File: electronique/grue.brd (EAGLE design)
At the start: 160 x 100 mm, 23 parts, among them IC3 REG1117, Q1 BSS138, Q2 BSS138

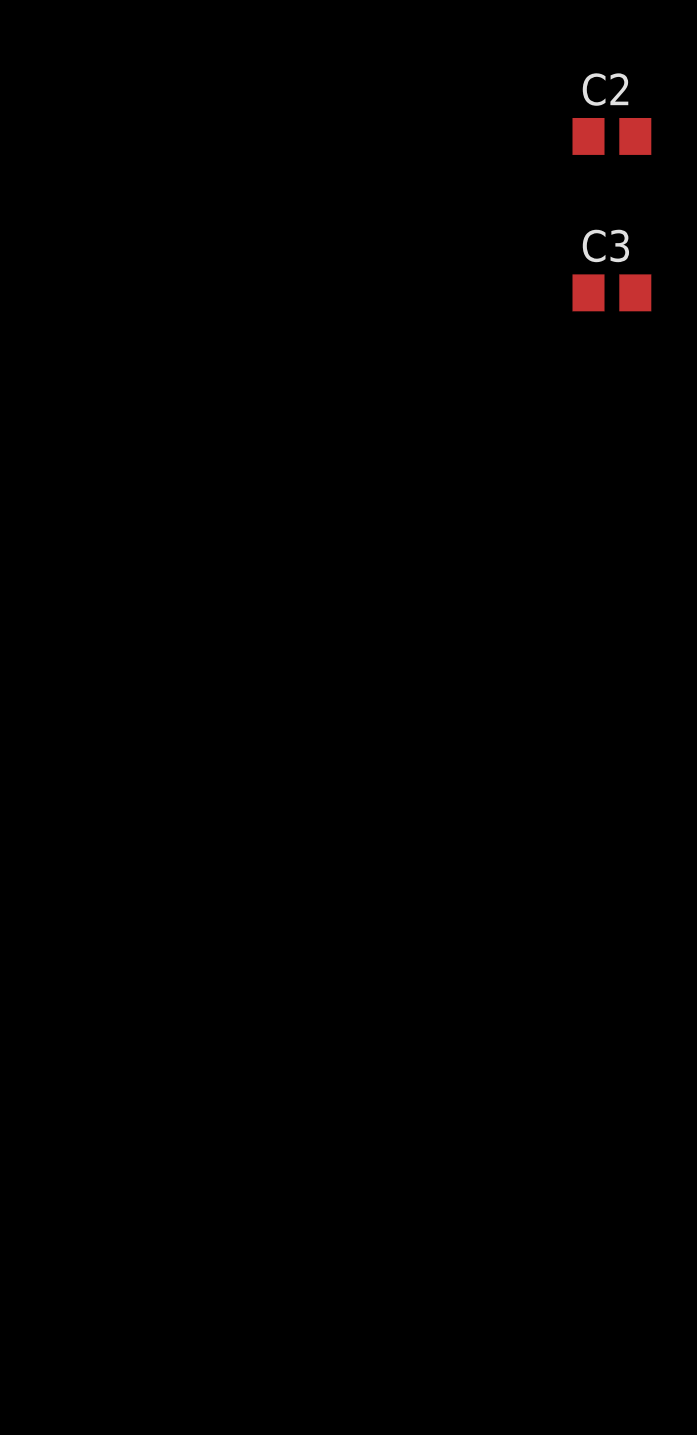
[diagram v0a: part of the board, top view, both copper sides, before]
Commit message: Ajout lib Eagle DC-DC-converter
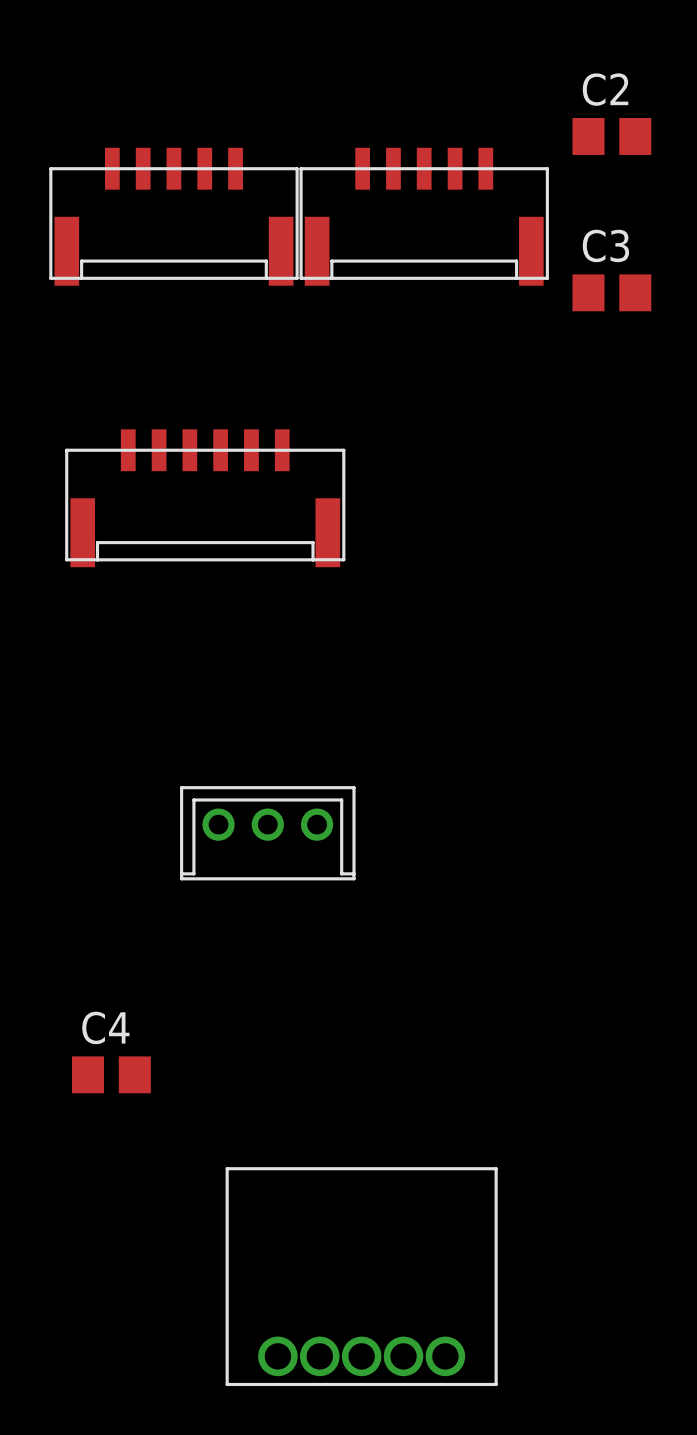
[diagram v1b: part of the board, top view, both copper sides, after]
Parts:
- added 12V->6V: DC-DC-CONVERTER, dc-dc-converter:DC-DC-CONVERTER
- added C4: 1µF, resistor:C0805
- added TOF_LP_D, TOF_LP_G: JST-05, con-jst:GH-05-V
- added TOF_PINCE: JST-06, con-jst:GH-06-V
- added XL320_G1: DYNAMIXEL-1X03XL, 1NTech_pinhead:DYNAMIXEL_XL_1X03
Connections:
- removed net 3.3V: U$1.3.3V
- removed net AGND: U$1.AGND
- new net N$1: U$1.0
- new net N$2: U$1.1
- new net VOUT: 12V->6V.VOUT
- net +3V3: now also U$1.3.3V
- net +6V: now also C4.1, XL320_G1.VCC
- net GND: now also 12V->6V.GND, C4.2, U$1.AGND, XL320_G1.GND
- net SERIAL_XL320_5V: now also XL320_G1.DATA
- net VIN: now also 12V->6V.VIN
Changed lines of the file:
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@@
 <?xml version="1.0" encoding="utf-8"?>
 <!DOCTYPE eagle SYSTEM "eagle.dtd">
-<eagle version="8.5.1">
+<eagle version="8.5.2">
 <drawing>
 <settings>
@@
 <attribute name="OC_FARNELL" value="1097566" x="-38.1" y="-152.4" size="1.778" layer="27" display="off"/>
 <attribute name="OC_NEWARK" value="14P6981" x="-38.1" y="-152.4" size="1.778" layer="27" display="off"/>
+<attribute name="RS" value="885-5432" x="-38.1" y="-152.4" size="1.778" layer="27" display="off"/>
 </element>
 <element name="C2" library="resistor" library_urn="urn:adsk.eagle:library:348" package="C0805" package3d_urn="urn:adsk.eagle:package:26137/1" value="10µF" x="-43.18" y="-162.56"/>
 <element name="C3" library="resistor" library_urn="urn:adsk.eagle:library:348" package="C0805" package3d_urn="urn:adsk.eagle:package:26137/1" value="22µF" x="-43.18" y="-168.91"/>
+<element name="TOF_LP_G" library="con-jst" package="GH-05-V" value="JST-05" x="-50.8" y="-166.37"/>
+<element name="TOF_LP_D" library="con-jst" package="GH-05-V" value="JST-05" x="-60.96" y="-166.37"/>
+<element name="TOF_PINCE" library="con-jst" package="GH-06-V" value="JST-06" x="-59.69" y="-177.8"/>
+<element name="XL320_G1" library="1NTech_pinhead" package="DYNAMIXEL_XL_1X03" value="DYNAMIXEL-1X03XL" x="-57.15" y="-190.5"/>
+<element name="C4" library="resistor" library_urn="urn:adsk.eagle:library:348" package="C0805" package3d_urn="urn:adsk.eagle:package:26137/1" value="1µF" x="-63.5" y="-200.66"/>
+<element name="12V-&gt;6V" library="dc-dc-converter" package="DC-DC-CONVERTER" value="DC-DC-CONVERTER" x="-53.34" y="-212.09"/>
 </elements>
 <signals>
@@
 <contactref element="C2" pad="2"/>
 <contactref element="C3" pad="2"/>
+<contactref element="U$1" pad="AGND"/>
+<contactref element="XL320_G1" pad="GND"/>
+<contactref element="C4" pad="2"/>
+<contactref element="12V-&gt;6V" pad="GND"/>
+<wire x1="-62.55" y1="-200.66" x2="-59.15" y2="-190.5" width="0" layer="19" extent="1-1"/>
+<wire x1="-53.34" y1="-212.09" x2="-62.55" y2="-200.66" width="0" layer="19" extent="1-1"/>
+<wire x1="-42.23" y1="-168.91" x2="-59.15" y2="-190.5" width="0" layer="19" extent="1-1"/>
 <wire x1="-42.23" y1="-162.56" x2="-42.23" y2="-168.91" width="0" layer="19" extent="1-1"/>
 <wire x1="-40.3606" y1="-155.5496" x2="-42.23" y2="-162.56" width="0" layer="19" extent="1-1"/>
@@
 <wire x1="-39.955" y1="-7.66" x2="-38.705" y2="-7.66" width="0" layer="19" extent="1-1"/>
 <wire x1="-15.56" y1="-24.13" x2="-34.61" y2="-24.13" width="0" layer="19" extent="1-1"/>
-<wire x1="-38.1" y1="35.56" x2="-37.455" y2="-7.66" width="0" layer="19" extent="1-1"/>
-</signal>
-<signal name="AGND">
-<contactref element="U$1" pad="AGND"/>
-</signal>
-<signal name="3.3V">
-<contactref element="U$1" pad="3.3V"/>
+<wire x1="-22.86" y1="33.02" x2="-36.205" y2="-7.66" width="0" layer="19" extent="1-1"/>
+<wire x1="-38.1" y1="35.56" x2="-22.86" y2="33.02" width="0" layer="19" extent="1-1"/>
 </signal>
 <signal name="AREF">
@@
 <signal name="VIN">
 <contactref element="U$1" pad="VIN"/>
+<contactref element="12V-&gt;6V" pad="VIN"/>
+<wire x1="-55.04" y1="-212.09" x2="-22.86" y2="35.56" width="0" layer="19" extent="1-1"/>
 </signal>
 <signal name="+12V">
@@
 <contactref element="T3" pad="C"/>
 <contactref element="T1" pad="C"/>
+<contactref element="U$1" pad="3.3V"/>
 <wire x1="-36.83" y1="-72.56" x2="-31.75" y2="-99.06" width="0" layer="19" extent="1-1"/>
 <wire x1="-41.91" y1="-72.56" x2="-36.83" y2="-72.56" width="0" layer="19" extent="1-1"/>
@@
 <wire x1="-18.73" y1="-53.17" x2="-26.35" y2="-53.17" width="0" layer="19" extent="1-1"/>
 <wire x1="-11.11" y1="-52.07" x2="-18.73" y2="-53.17" width="0" layer="19" extent="1-1"/>
+<wire x1="-22.86" y1="30.48" x2="-11.11" y2="-52.07" width="0" layer="19" extent="1-1"/>
 </signal>
 <signal name="+6V">
 <contactref element="XL320_G" pad="VCC"/>
 <contactref element="C7" pad="1"/>
+<contactref element="XL320_G1" pad="VCC"/>
+<contactref element="C4" pad="1"/>
+<wire x1="-64.45" y1="-200.66" x2="-57.15" y2="-190.5" width="0" layer="19" extent="1-1"/>
+<wire x1="-36.83" y1="-55.88" x2="-57.15" y2="-190.5" width="0" layer="19" extent="1-1"/>
 <wire x1="-17.46" y1="-24.13" x2="-36.83" y2="-55.88" width="0" layer="19" extent="1-1"/>
 </signal>
@@
 <contactref element="R7" pad="2"/>
 <contactref element="XL320_G" pad="DATA"/>
+<contactref element="XL320_G1" pad="DATA"/>
+<wire x1="-32.07" y1="-66.04" x2="-55.15" y2="-190.5" width="0" layer="19" extent="1-1"/>
 <wire x1="-34.83" y1="-55.88" x2="-32.07" y2="-66.04" width="0" layer="19" extent="1-1"/>
 <wire x1="-17.78" y1="-50.97" x2="-34.83" y2="-55.88" width="0" layer="19" extent="1-1"/>
@@
 <wire x1="-42.86" y1="-74.76" x2="-35.88" y2="-81.28" width="0" layer="19" extent="1-1"/>
 </signal>
+<signal name="N$1">
+<contactref element="U$1" pad="0"/>
+</signal>
+<signal name="N$2">
+<contactref element="U$1" pad="1"/>
+</signal>
+<signal name="VOUT">
+<contactref element="12V-&gt;6V" pad="VOUT"/>
+</signal>
 </signals>

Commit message: Carte secondaire : schéma presque fini, il manque juste 2 pins à la teensy... :'(
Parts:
- removed 12V->6V: DC-DC-CONVERTER, dc-dc-converter:DC-DC-CONVERTER
- added C6: 1µF, resistor:C0805
- added DC-DC-6V: DC-DC-CONVERTER, dc-dc-converter-6v:DC-DC-CONVERTER
- added GYRO: JST-04GH-V, con-jst:GH-04-V
- added H-BRIDGE_H:C1, H-BRIDGE_H:C2, H-BRIDGE_V:C1, H-BRIDGE_V:C2: 100nF, resistor:C0805
- added H-BRIDGE_H:D1, H-BRIDGE_H:D2, H-BRIDGE_H:D3, H-BRIDGE_H:D4, H-BRIDGE_V:D1, H-BRIDGE_V:D2, H-BRIDGE_V:D3, H-BRIDGE_V:D4: S1M, diode:SMA
- added H-BRIDGE_H:IC1, H-BRIDGE_V:IC1: L298, st-microelectronics:MULTIWATT-15
- added H-BRIDGE_H:R1, H-BRIDGE_H:R2, H-BRIDGE_H:R3, H-BRIDGE_V:R1, H-BRIDGE_V:R2, H-BRIDGE_V:R3, R10, R4, R5, R8, R9: 10k, resistor:R0805
- added MOT_H, MOT_V: (no value), pinhead:1X06
- added R1: 220, resistor:R0805
- added U$2, U$3, U$4, U$5, U$6: PUSH-BUTTON, push-button:PUSH-BUTTON
- renumbered TOF_LP_D to TOF_LP_D_AND_DISPLAY
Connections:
- removed net N$2: U$1.1
- removed net VOUT: 12V->6V.VOUT
- new net MOT_H_EN: H-BRIDGE_H:IC1.11, H-BRIDGE_H:IC1.6, H-BRIDGE_H:R1.1, U$1.3
- new net MOT_H_ENC_A: MOT_H.5
- new net MOT_H_ENC_B: MOT_H.6
- new net MOT_H_IN1: H-BRIDGE_H:IC1.12, H-BRIDGE_H:IC1.5, H-BRIDGE_H:R2.1, U$1.4
- new net MOT_H_IN2: H-BRIDGE_H:IC1.10, H-BRIDGE_H:IC1.7, H-BRIDGE_H:R3.1, U$1.5
- new net MOT_H_OUT+: H-BRIDGE_H:D1.C, H-BRIDGE_H:D2.A, H-BRIDGE_H:IC1.14, H-BRIDGE_H:IC1.2, MOT_H.1
- new net MOT_H_OUT-: H-BRIDGE_H:D3.A, H-BRIDGE_H:D4.C, H-BRIDGE_H:IC1.13, H-BRIDGE_H:IC1.3, MOT_H.2
- new net MOT_V_EN: H-BRIDGE_V:IC1.11, H-BRIDGE_V:IC1.6, H-BRIDGE_V:R1.1, U$1.21/A7
- new net MOT_V_ENC_A: MOT_V.5
- new net MOT_V_ENC_B: MOT_V.6
- new net MOT_V_IN1: H-BRIDGE_V:IC1.12, H-BRIDGE_V:IC1.5, H-BRIDGE_V:R2.1, U$1.22/A8
- new net MOT_V_IN2: H-BRIDGE_V:IC1.10, H-BRIDGE_V:IC1.7, H-BRIDGE_V:R3.1, U$1.23/A9
- new net MOT_V_OUT+: H-BRIDGE_V:D1.C, H-BRIDGE_V:D2.A, H-BRIDGE_V:IC1.14, H-BRIDGE_V:IC1.2, MOT_V.1
- new net MOT_V_OUT-: H-BRIDGE_V:D3.A, H-BRIDGE_V:D4.C, H-BRIDGE_V:IC1.13, H-BRIDGE_V:IC1.3, MOT_V.2
- new net N$13: R5.2, U$1.13, U$2.3, U$2.4
- new net N$14: R8.2, U$1.14/A0, U$3.3, U$3.4
- new net N$15: R9.1, U$1.15/A1, U$4.3, U$4.4
- new net N$16: R10.1, U$1.16/A2, U$5.3, U$5.4
- new net N$3: DC-DC-6V.TRIM+, R1.2
- new net SCL: TOF_LP_D_AND_DISPLAY.4, TOF_LP_G.4, TOF_PINCE.4, U$1.19/A5
- new net SDA: TOF_LP_D_AND_DISPLAY.3, TOF_LP_G.3, TOF_PINCE.3, U$1.18/A4
- new net TOF_LP_D: TOF_LP_D_AND_DISPLAY.5, U$1.11
- new net TOF_LP_G: TOF_LP_G.5, U$1.2
- new net TOF_PINCE_EXT: TOF_PINCE.6, U$1.17/A3
- new net TOF_PINCE_INT: TOF_PINCE.5, U$1.12
- net +12V: now also DC-DC-6V.VIN
- net +3V3: now also R10.2, R4.2, R5.1, R8.1, R9.2, TOF_LP_D_AND_DISPLAY.2, TOF_LP_G.2, TOF_PINCE.2
- net +5V: now also H-BRIDGE_H:C2.2, H-BRIDGE_H:IC1.9, H-BRIDGE_V:C2.2, H-BRIDGE_V:IC1.9, MOT_H.4, MOT_V.4
- net +6V: now also DC-DC-6V.VOUT, H-BRIDGE_H:C1.2, H-BRIDGE_H:D2.C, H-BRIDGE_H:D3.C, H-BRIDGE_H:IC1.4, H-BRIDGE_V:C1.2, H-BRIDGE_V:D2.C, H-BRIDGE_V:D3.C, H-BRIDGE_V:IC1.4
- net DEL_GYRO_1: now also GYRO.1
- net DEL_GYRO_1_PWM: now also U$1.6
- net DEL_GYRO_2: now also GYRO.3
- net DEL_GYRO_2_PWM: now also U$1.20/A6
- net GND: now also C6.1, DC-DC-6V.GND, GYRO.2, GYRO.4, H-BRIDGE_H:C1.1, H-BRIDGE_H:C2.1, H-BRIDGE_H:D1.A, H-BRIDGE_H:D4.A, H-BRIDGE_H:IC1.1, H-BRIDGE_H:IC1.15, H-BRIDGE_H:IC1.8, H-BRIDGE_H:R1.2, H-BRIDGE_H:R2.2, H-BRIDGE_H:R3.2, H-BRIDGE_V:C1.1, H-BRIDGE_V:C2.1, H-BRIDGE_V:D1.A, H-BRIDGE_V:D4.A, H-BRIDGE_V:IC1.1, H-BRIDGE_V:IC1.15, H-BRIDGE_V:IC1.8, H-BRIDGE_V:R1.2, H-BRIDGE_V:R2.2, H-BRIDGE_V:R3.2, MOT_H.3, MOT_V.3, R1.1, TOF_LP_D_AND_DISPLAY.1, TOF_LP_G.1, TOF_PINCE.1, U$2.1, U$2.2, U$3.1, U$3.2, U$4.1, U$4.2, U$5.1, U$5.2, U$6.3, U$6.4; no longer 12V->6V.GND
- net GRUE_SERIAL_MISO: now also U$1.1
- net GRUE_SERIAL_MOSI: now also U$1.0
- net N$1: now also C6.2, R4.1, U$1.A10, U$6.1, U$6.2; no longer U$1.0
- net SERIAL_AX12: now also U$1.10, U$1.9
- net SERIAL_XL320: now also U$1.7, U$1.8
- net VIN: no longer 12V->6V.VIN

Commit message: Comment ça il n'y a plus de pins dispo ? mais enfin tout va bien !
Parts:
- removed C6: 1µF, resistor:C0805
- removed R10, R4, R5, R8, R9: 10k, resistor:R0805
- removed U$2, U$3, U$4, U$5, U$6: PUSH-BUTTON, push-button:PUSH-BUTTON
- added MULTI-BUTTON-1:C1, MULTI-BUTTON-2:C1: 1µF, resistor:C0805
- added MULTI-BUTTON-1:R1, MULTI-BUTTON-2:R1: 4k7, resistor:R0805
- added MULTI-BUTTON-1:R2, MULTI-BUTTON-2:R2: 2k2, resistor:R0805
- added MULTI-BUTTON-1:R3, MULTI-BUTTON-2:R3: 10k, resistor:R0805
- added MULTI-BUTTON-1:U1, MULTI-BUTTON-1:U2, MULTI-BUTTON-1:U3, MULTI-BUTTON-2:U1, MULTI-BUTTON-2:U2, MULTI-BUTTON-2:U3: PUSH-BUTTON, push-button:PUSH-BUTTON
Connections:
- removed net N$13: R5.2, U$1.13, U$2.3, U$2.4
- removed net N$14: R8.2, U$1.14/A0, U$3.3, U$3.4
- removed net N$15: R9.1, U$1.15/A1, U$4.3, U$4.4
- removed net N$16: R10.1, U$1.16/A2, U$5.3, U$5.4
- new net MULTI-BUTTON-1:N$3: MULTI-BUTTON-1:R2.1, MULTI-BUTTON-1:U2.3, MULTI-BUTTON-1:U2.4
- new net MULTI-BUTTON-1:N$4: MULTI-BUTTON-1:R3.1, MULTI-BUTTON-1:U1.3, MULTI-BUTTON-1:U1.4
- new net MULTI-BUTTON-2:N$3: MULTI-BUTTON-2:R2.1, MULTI-BUTTON-2:U2.3, MULTI-BUTTON-2:U2.4
- new net MULTI-BUTTON-2:N$4: MULTI-BUTTON-2:R3.1, MULTI-BUTTON-2:U1.3, MULTI-BUTTON-2:U1.4
- new net N$2: MULTI-BUTTON-2:C1.2, MULTI-BUTTON-2:R1.2, MULTI-BUTTON-2:U1.1, MULTI-BUTTON-2:U1.2, MULTI-BUTTON-2:U2.1, MULTI-BUTTON-2:U2.2, MULTI-BUTTON-2:U3.1, MULTI-BUTTON-2:U3.2, U$1.A11
- net +3V3: now also MULTI-BUTTON-1:R1.1, MULTI-BUTTON-2:R1.1; no longer R10.2, R4.2, R5.1, R8.1, R9.2
- net GND: now also MULTI-BUTTON-1:C1.1, MULTI-BUTTON-1:R2.2, MULTI-BUTTON-1:R3.2, MULTI-BUTTON-1:U3.3, MULTI-BUTTON-1:U3.4, MULTI-BUTTON-2:C1.1, MULTI-BUTTON-2:R2.2, MULTI-BUTTON-2:R3.2, MULTI-BUTTON-2:U3.3, MULTI-BUTTON-2:U3.4; no longer C6.1, U$2.1, U$2.2, U$3.1, U$3.2, U$4.1, U$4.2, U$5.1, U$5.2, U$6.3, U$6.4
- net MOT_H_ENC_A: now also U$1.11
- net MOT_H_ENC_B: now also U$1.12
- net MOT_V_ENC_A: now also U$1.15/A1
- net MOT_V_ENC_B: now also U$1.16/A2
- net N$1: now also MULTI-BUTTON-1:C1.2, MULTI-BUTTON-1:R1.2, MULTI-BUTTON-1:U1.1, MULTI-BUTTON-1:U1.2, MULTI-BUTTON-1:U2.1, MULTI-BUTTON-1:U2.2, MULTI-BUTTON-1:U3.1, MULTI-BUTTON-1:U3.2; no longer C6.2, R4.1, U$6.1, U$6.2
- net TOF_LP_D: now also U$1.13; no longer U$1.11
- net TOF_PINCE_INT: now also U$1.14/A0; no longer U$1.12

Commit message: L'élec ça c'est fait !
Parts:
- removed H-BRIDGE_H:C1, H-BRIDGE_H:C2, H-BRIDGE_V:C1, H-BRIDGE_V:C2: 100nF, resistor:C0805
- removed H-BRIDGE_H:D1, H-BRIDGE_H:D2, H-BRIDGE_H:D3, H-BRIDGE_H:D4, H-BRIDGE_V:D1, H-BRIDGE_V:D2, H-BRIDGE_V:D3, H-BRIDGE_V:D4: S1M, diode:SMA
- removed H-BRIDGE_H:IC1, H-BRIDGE_V:IC1: L298, st-microelectronics:MULTIWATT-15
- removed H-BRIDGE_H:R1, H-BRIDGE_H:R2, H-BRIDGE_H:R3, H-BRIDGE_V:R1, H-BRIDGE_V:R2, H-BRIDGE_V:R3: 10k, resistor:R0805
- added F1: MF-LSMF300, polyswitch:MF-LSMF300
- added H-BRIDGE1:C1, H-BRIDGE1:C2: 100nF, resistor:C0805
- added H-BRIDGE1:D1, H-BRIDGE1:D2, H-BRIDGE1:D3, H-BRIDGE1:D4, H-BRIDGE1:D5, H-BRIDGE1:D6, H-BRIDGE1:D7, H-BRIDGE1:D8: S1M, diode:SMA
- added H-BRIDGE1:IC1: L298, st-microelectronics:MULTIWATT-15
- added H-BRIDGE1:R1, H-BRIDGE1:R2, H-BRIDGE1:R3, H-BRIDGE1:R4, H-BRIDGE1:R5, H-BRIDGE1:R6: 10k, resistor:R0805
- moved MULTI-BUTTON-2:U3 487.0 mm to (70.5, 14.0), flipped to the bottom, turned to 180 degrees
- moved MULTI-BUTTON-2:U2 480.0 mm to (59.5, 14.0), flipped to the bottom, turned to 180 degrees
- moved MULTI-BUTTON-2:U1 478.6 mm to (48.5, 19.5), flipped to the bottom, turned to 90 degrees
- moved MULTI-BUTTON-2:R1 475.9 mm to (56.0, 23.0), flipped to the bottom, turned to 270 degrees
- moved MULTI-BUTTON-2:R3 471.6 mm to (56.0, 6.00), flipped to the bottom, turned to 270 degrees
- moved MULTI-BUTTON-2:C1 470.2 mm to (40.0, 29.0), flipped to the bottom, turned to 270 degrees
- moved MULTI-BUTTON-2:R2 468.1 mm to (59.5, 7.00), flipped to the bottom, turned to 180 degrees
- moved MULTI-BUTTON-1:C1 461.2 mm to (42.5, 29.0), flipped to the bottom, turned to 270 degrees
- moved MULTI-BUTTON-1:R2 446.6 mm to (39.0, 21.0), flipped to the bottom
- moved MULTI-BUTTON-1:U2 442.2 mm to (37.5, 14.0), flipped to the bottom
- moved MULTI-BUTTON-1:U3 440.7 mm to (26.5, 14.0), flipped to the bottom
- moved MULTI-BUTTON-1:R3 429.5 mm to (45.0, 13.0), flipped to the bottom, turned to 180 degrees
- moved MULTI-BUTTON-1:R1 422.9 mm to (21.0, 8.00), flipped to the bottom, turned to 180 degrees
- moved MULTI-BUTTON-1:U1 415.6 mm to (48.5, 8.50), flipped to the bottom, turned to 270 degrees
- moved GYRO 365.2 mm to (26.0, 12.0), turned to 180 degrees
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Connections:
- new net N$4: F1.1, H-BRIDGE1:C1.2, H-BRIDGE1:D2.C, H-BRIDGE1:D3.C, H-BRIDGE1:D6.C, H-BRIDGE1:D7.C, H-BRIDGE1:IC1.4
- net +5V: now also H-BRIDGE1:C2.2, H-BRIDGE1:IC1.9; no longer H-BRIDGE_H:C2.2, H-BRIDGE_H:IC1.9, H-BRIDGE_V:C2.2, H-BRIDGE_V:IC1.9
- net +6V: now also F1.2; no longer H-BRIDGE_H:C1.2, H-BRIDGE_H:D2.C, H-BRIDGE_H:D3.C, H-BRIDGE_H:IC1.4, H-BRIDGE_V:C1.2, H-BRIDGE_V:D2.C, H-BRIDGE_V:D3.C, H-BRIDGE_V:IC1.4
- net GND: now also H-BRIDGE1:C1.1, H-BRIDGE1:C2.1, H-BRIDGE1:D1.A, H-BRIDGE1:D4.A, H-BRIDGE1:D5.A, H-BRIDGE1:D8.A, H-BRIDGE1:IC1.1, H-BRIDGE1:IC1.15, H-BRIDGE1:IC1.8, H-BRIDGE1:R1.2, H-BRIDGE1:R2.2, H-BRIDGE1:R3.2, H-BRIDGE1:R4.2, H-BRIDGE1:R5.2, H-BRIDGE1:R6.2; no longer H-BRIDGE_H:C1.1, H-BRIDGE_H:C2.1, H-BRIDGE_H:D1.A, H-BRIDGE_H:D4.A, H-BRIDGE_H:IC1.1, H-BRIDGE_H:IC1.15, H-BRIDGE_H:IC1.8, H-BRIDGE_H:R1.2, H-BRIDGE_H:R2.2, H-BRIDGE_H:R3.2, H-BRIDGE_V:C1.1, H-BRIDGE_V:C2.1, H-BRIDGE_V:D1.A, H-BRIDGE_V:D4.A, H-BRIDGE_V:IC1.1, H-BRIDGE_V:IC1.15, H-BRIDGE_V:IC1.8, H-BRIDGE_V:R1.2, H-BRIDGE_V:R2.2, H-BRIDGE_V:R3.2
- net MOT_H_EN: now also H-BRIDGE1:IC1.6, H-BRIDGE1:R1.1; no longer H-BRIDGE_H:IC1.11, H-BRIDGE_H:IC1.6, H-BRIDGE_H:R1.1
- net MOT_H_IN1: now also H-BRIDGE1:IC1.5, H-BRIDGE1:R3.1; no longer H-BRIDGE_H:IC1.12, H-BRIDGE_H:IC1.5, H-BRIDGE_H:R2.1
- net MOT_H_IN2: now also H-BRIDGE1:IC1.7, H-BRIDGE1:R4.1; no longer H-BRIDGE_H:IC1.10, H-BRIDGE_H:IC1.7, H-BRIDGE_H:R3.1
- net MOT_H_OUT+: now also H-BRIDGE1:D1.C, H-BRIDGE1:D2.A, H-BRIDGE1:IC1.2; no longer H-BRIDGE_H:D1.C, H-BRIDGE_H:D2.A, H-BRIDGE_H:IC1.14, H-BRIDGE_H:IC1.2
- net MOT_H_OUT-: now also H-BRIDGE1:D3.A, H-BRIDGE1:D4.C, H-BRIDGE1:IC1.3; no longer H-BRIDGE_H:D3.A, H-BRIDGE_H:D4.C, H-BRIDGE_H:IC1.13, H-BRIDGE_H:IC1.3
- net MOT_V_EN: now also H-BRIDGE1:IC1.11, H-BRIDGE1:R2.1; no longer H-BRIDGE_V:IC1.11, H-BRIDGE_V:IC1.6, H-BRIDGE_V:R1.1
- net MOT_V_IN1: now also H-BRIDGE1:IC1.10, H-BRIDGE1:R5.1; no longer H-BRIDGE_V:IC1.12, H-BRIDGE_V:IC1.5, H-BRIDGE_V:R2.1
- net MOT_V_IN2: now also H-BRIDGE1:IC1.12, H-BRIDGE1:R6.1; no longer H-BRIDGE_V:IC1.10, H-BRIDGE_V:IC1.7, H-BRIDGE_V:R3.1
- net MOT_V_OUT+: now also H-BRIDGE1:D5.C, H-BRIDGE1:D6.A, H-BRIDGE1:IC1.13; no longer H-BRIDGE_V:D1.C, H-BRIDGE_V:D2.A, H-BRIDGE_V:IC1.14, H-BRIDGE_V:IC1.2
- net MOT_V_OUT-: now also H-BRIDGE1:D7.A, H-BRIDGE1:D8.C, H-BRIDGE1:IC1.14; no longer H-BRIDGE_V:D3.A, H-BRIDGE_V:D4.C, H-BRIDGE_V:IC1.13, H-BRIDGE_V:IC1.3
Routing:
- net +6V: track 0.00 -> 190.3 mm, vias 0 -> 2
- net +3V3: track 0.00 -> 141.4 mm, vias 0 -> 9
- net +12V: track 0.00 -> 104.1 mm, vias 0 -> 3
- net +5V: track 0.00 -> 95.3 mm, vias 0 -> 3
- net SDA: track 0.00 -> 80.0 mm, vias 0 -> 4
- net SERIAL_XL320_5V: track 0.00 -> 77.0 mm, vias 0 -> 2
- net N$1: track 0.00 -> 74.9 mm, vias 0 -> 1
- net MOT_H_EN: track 0.00 -> 70.3 mm, vias 0 -> 1
- net SCL: track 0.00 -> 69.8 mm, vias 0 -> 4
- net N$2: track 0.00 -> 67.0 mm
- net TOF_LP_G: track 0.00 -> 64.5 mm, vias 0 -> 2
- net MOT_V_IN2: track 0.00 -> 59.9 mm, vias 0 -> 1
- net MOT_H_IN1: track 0.00 -> 59.3 mm, vias 0 -> 1
- net MOT_V_IN1: track 0.00 -> 58.0 mm, vias 0 -> 1
- net MOT_H_IN2: track 0.00 -> 54.9 mm, vias 0 -> 1
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- added copper zone on layer 1, net GND
- added copper zone on layer 16, net GND
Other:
- board size 160 x 100 mm -> 90.5 x 48.5 mm
